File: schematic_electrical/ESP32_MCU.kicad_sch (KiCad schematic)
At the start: 14 parts, among them U1 ESP32_S2_PICO

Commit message: delete button4
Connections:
- net at U1.18 (IO16/A15): no longer R11.2
- net at U1.20 (IO15/A14): now also R11.2; no longer R14.2
- net at U1.22 (IO14/A13): now also R14.2; no longer R15.2
- net at U1.24 (IO13/A12): now also R15.2
- net BUTTON4_ESP3V3: no longer names the net of U1.13 (IO7/A6)
- no-connect marks 10 -> 11
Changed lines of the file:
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@@
+	)
+	(no_connect
+		(at 180.34 81.28)
 	)
 	(no_connect
@@
 	(wire
 		(pts
-			(xy 266.7 86.36) (xy 266.7 92.71)
-		)
-		(stroke
-			(width 0)
-			(type default)
-		)
-	)
-	(wire
-		(pts
 			(xy 266.7 107.95) (xy 266.7 110.49)
 		)
@@
 	(wire
 		(pts
+			(xy 180.34 88.9) (xy 266.7 88.9)
+		)
+		(stroke
+			(width 0)
+			(type default)
+		)
+	)
+	(wire
+		(pts
 			(xy 161.29 119.38) (xy 161.29 146.05)
 		)
@@
 	(wire
 		(pts
-			(xy 180.34 81.28) (xy 231.14 81.28)
-		)
-		(stroke
-			(width 0)
-			(type default)
-		)
-	)
-	(wire
-		(pts
 			(xy 82.55 63.5) (xy 82.55 60.96)
 		)
@@
 	(wire
 		(pts
-			(xy 231.14 81.28) (xy 231.14 92.71)
+			(xy 180.34 83.82) (xy 231.14 83.82)
 		)
 		(stroke
@@
 	(wire
 		(pts
+			(xy 231.14 83.82) (xy 231.14 92.71)
+		)
+		(stroke
+			(width 0)
+			(type default)
+		)
+	)
+	(wire
+		(pts
 			(xy 180.34 99.06) (xy 185.42 99.06)
 		)
@@
 	(wire
 		(pts
-			(xy 180.34 83.82) (xy 248.92 83.82)
-		)
-		(stroke
-			(width 0)
-			(type default)
-		)
-	)
-	(wire
-		(pts
 			(xy 80.01 118.11) (xy 80.01 115.57)
 		)
@@
 	(wire
 		(pts
-			(xy 248.92 83.82) (xy 248.92 92.71)
-		)
-		(stroke
-			(width 0)
-			(type default)
-		)
-	)
-	(wire
-		(pts
 			(xy 140.97 63.5) (xy 142.24 63.5)
 		)
@@
 	(wire
 		(pts
-			(xy 137.16 76.2) (xy 142.24 76.2)
+			(xy 266.7 88.9) (xy 266.7 92.71)
 		)
 		(stroke
@@
 	(wire
 		(pts
-			(xy 137.16 43.18) (xy 193.04 43.18)
+			(xy 180.34 86.36) (xy 248.92 86.36)
 		)
 		(stroke
@@
 	(wire
 		(pts
-			(xy 180.34 86.36) (xy 266.7 86.36)
-		)
-		(stroke
-			(width 0)
-			(type default)
-		)
-	)
-	(wire
-		(pts
 			(xy 129.54 78.74) (xy 129.54 76.2)
 		)
@@
 	(wire
 		(pts
+			(xy 248.92 86.36) (xy 248.92 92.71)
+		)
+		(stroke
+			(width 0)
+			(type default)
+		)
+	)
+	(wire
+		(pts
 			(xy 161.29 146.05) (xy 176.53 146.05)
 		)
@@
 		(pts
 			(xy 63.5 125.73) (xy 63.5 127)
-		)
-		(stroke
-			(width 0)
-			(type default)
-		)
-	)
-	(wire
-		(pts
-			(xy 137.16 43.18) (xy 137.16 76.2)
 		)
 		(stroke
@@
 			(effects
 				(font
-					(size 1.27 1.27)
-				)
-				(justify left)
-				(hide yes)
-			)
-		)
-	)
-	(global_label "BUTTON4_ESP3V3"
-		(shape input)
-		(at 193.04 43.18 0)
-		(fields_autoplaced yes)
-		(effects
-			(font
-				(size 1.27 1.27)
-			)
-			(justify left)
-		)
-		(property "Intersheetrefs" "${INTERSHEET_REFS}"
-			(at 204.4314 43.18 0)
-			(effects
-				(font

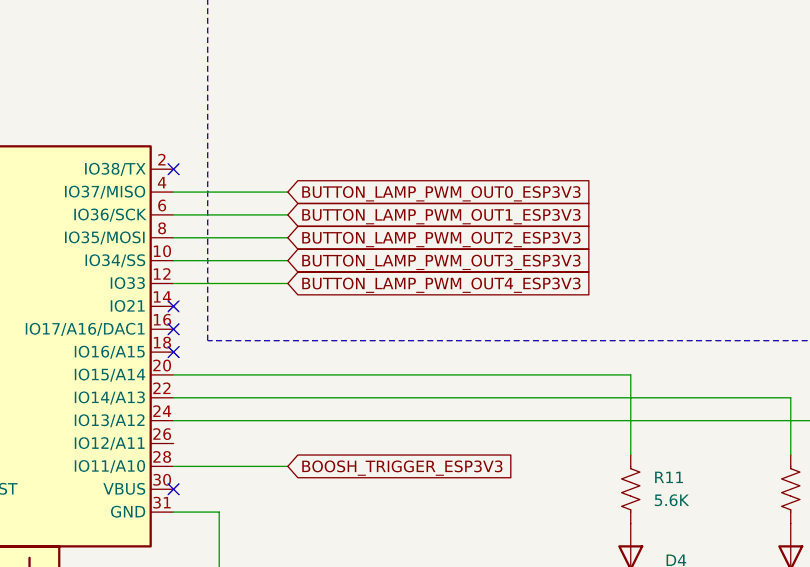
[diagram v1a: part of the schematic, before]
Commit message: Schematic for bar: use ULN2308 for button 12V lamps
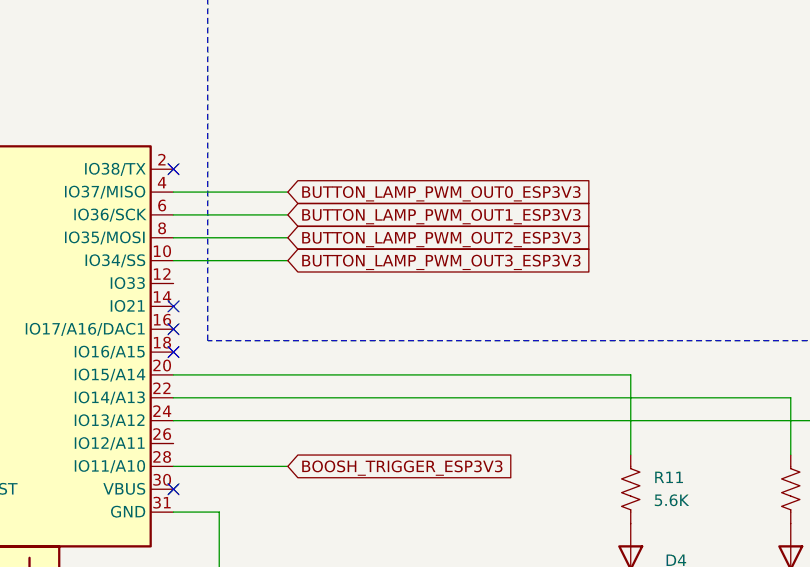
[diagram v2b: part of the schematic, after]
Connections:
- net BUTTON_LAMP_PWM_OUT4_ESP3V3: no longer names the net of U1.12 (IO33)
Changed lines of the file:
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@@
-	(wire
-		(pts
-			(xy 180.34 73.66) (xy 193.04 73.66)
-		)
-		(stroke
-			(width 0)
-			(type default)
-		)
-	)
 	(wire
 		(pts
@@
 			(effects
 				(font
-					(size 1.27 1.27)
-				)
-				(justify left)
-				(hide yes)
-			)
-		)
-	)
-	(global_label "BUTTON_LAMP_PWM_OUT4_ESP3V3"
-		(shape input)
-		(at 193.04 73.66 0)
-		(fields_autoplaced yes)
-		(effects
-			(font
-				(size 1.27 1.27)
-			)
-			(justify left)
-		)
-		(property "Intersheetrefs" "${INTERSHEET_REFS}"
-			(at 228.0774 73.66 0)
-			(effects
-				(font
